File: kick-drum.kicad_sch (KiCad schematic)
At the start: 68 parts, among them J1 Conn_02x05_Odd_Even, J2 GATE, J3 ACCENT CV, J4 PITCH CV, J5 OUTPUT, M1 Standoff, M2 Standoff, M3 Screw, M4 Screw, M5 Screw, M6 Screw, Q1 BCM857DS,135, Q2 BC547C, Q3 BCM847DS,135, U1 TL074

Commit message: update footprints
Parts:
- removed H5, H6, H7, H8: Standoff, MountingHole:MountingHole_2.7mm_M2.5, symbol Mechanical:MountingHole
- removed M1, M2: Standoff, Eurorack:Standoff_M2.5x0.45-11mm, symbol Eurorack:Standoff
- removed M3, M4, M5, M6: Screw, Eurorack:Screw_M2.5x0.45-6mm, symbol Eurorack:Screw
- C10, C3, C4, C7, C8: footprint (none) -> Capacitor_SMD:C_0805_2012Metric
- C5, C6, C9: footprint (none) -> Capacitor_THT:C_Rect_L7.2mm_W3.5mm_P5.00mm_FKS2_FKP2_MKS2_MKP2
- D3, D4, D5, D6, D7: footprint (none) -> Diode_SMD:D_SOD-323_HandSoldering
- J2, J3, J4, J5: footprint (none) -> Eurorack:AudioJack2_Tayda_A-2566
- Q1, Q3: footprint (none) -> Package_SO:TSOP-6_1.65x3.05mm_P0.95mm
- Q2: footprint (none) -> Package_TO_SOT_THT:TO-92_Inline_Wide
- R10, R11, R12, R13, R14, R15, R16, R17, R18, R19, R20, R21, R3, R4, R5, R6, R7, R8, R9: footprint (none) -> Resistor_SMD:R_0805_2012Metric
- RV1, RV5, RV6, RV7: footprint (none) -> Eurorack:Potentiometer_RV16AF-41-15R1
- RV2, RV3, RV4: footprint (none) -> Potentiometer_THT:Potentiometer_Bourns_3296W_Vertical
- U1: footprint (none) -> Package_SO:SOIC-14-16_3.9x9.9mm_P1.27mm
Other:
- note removed: "Mechanical attachment for 3 layer module"

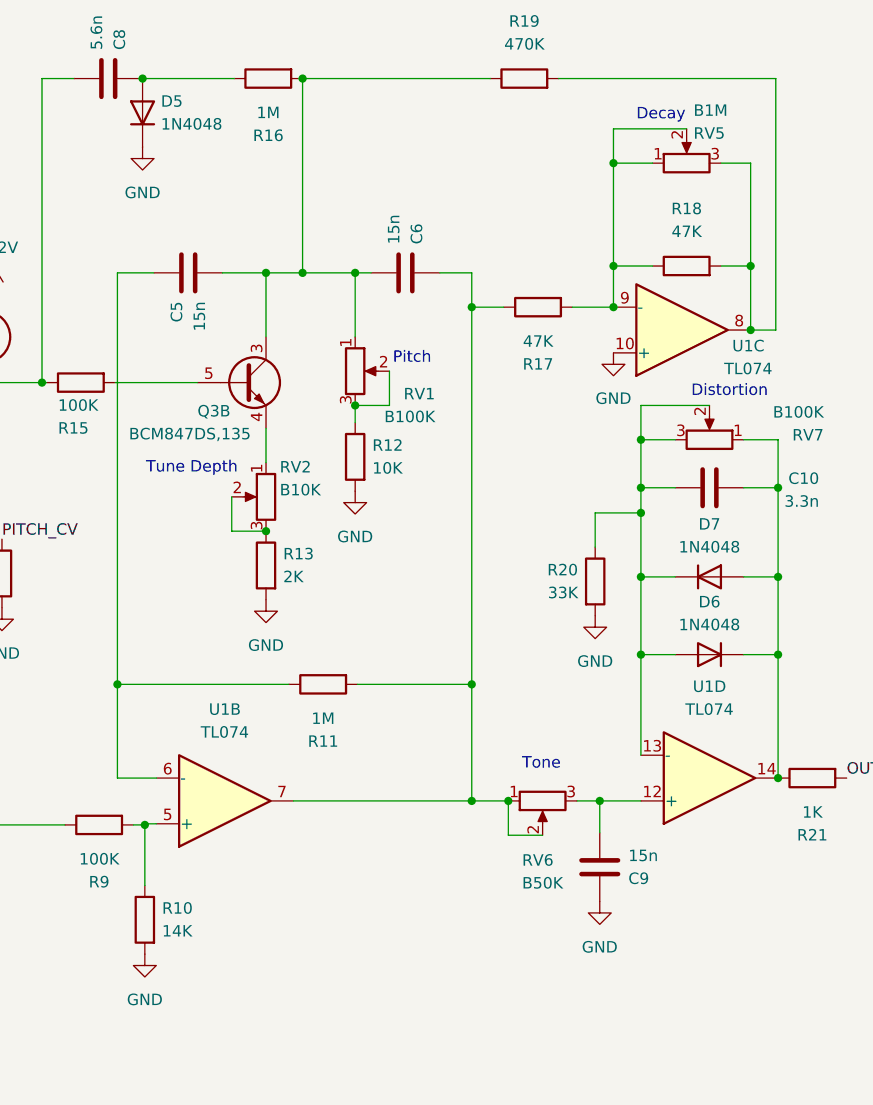
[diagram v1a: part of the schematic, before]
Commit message: update 15n caps to box type
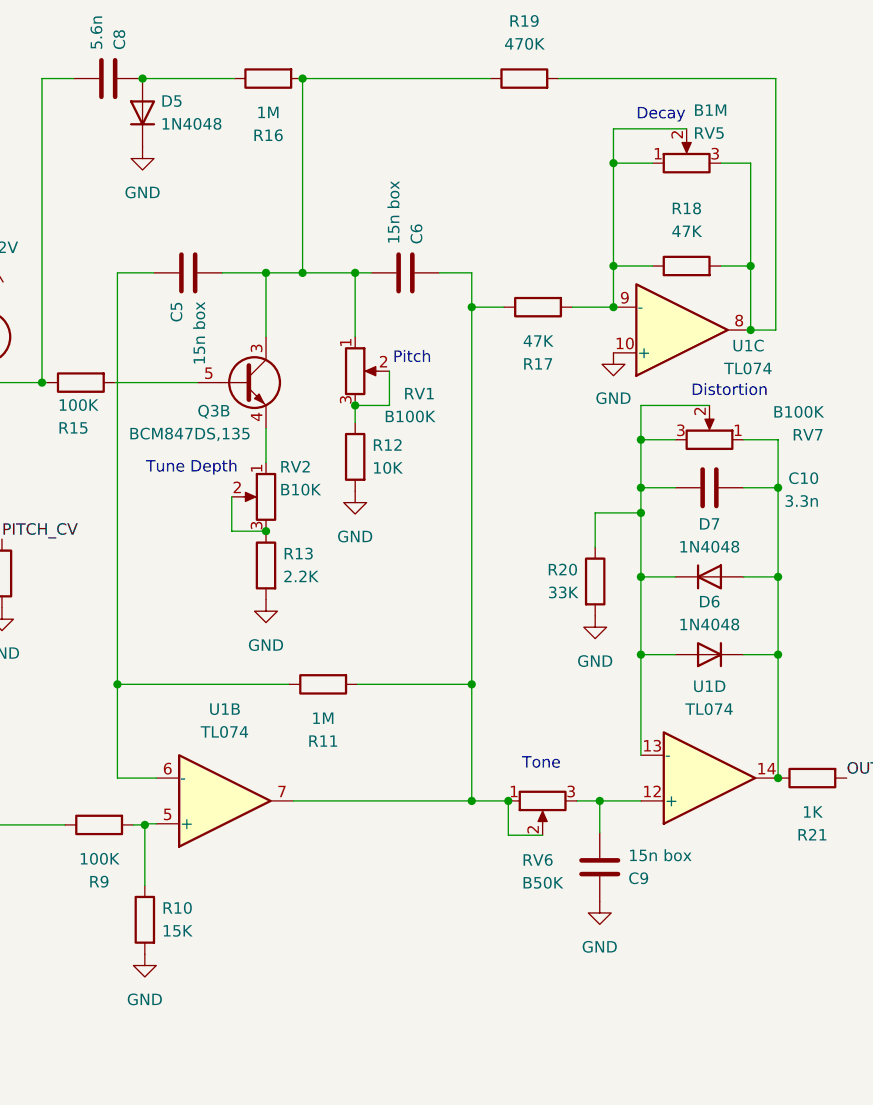
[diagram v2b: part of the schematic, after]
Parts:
- C5, C6, C9: value 15n -> 15n box
- R10: value 14K -> 15K
- R13: value 2K -> 2.2K
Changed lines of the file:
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@@
       (effects (font (size 1.27 1.27)) (justify right))
     )
-    (property "Value" "14K" (at 161.671 125.984 0)
+    (property "Value" "15K" (at 161.671 125.984 0)
       (effects (font (size 1.27 1.27)) (justify right))
     )
@@
       (effects (font (size 1.27 1.27)) (justify right))
     )
-    (property "Value" "15n" (at 187.452 49.657 0)
+    (property "Value" "15n box" (at 187.452 49.657 0)
       (effects (font (size 1.27 1.27)) (justify right))
     )
@@
       (effects (font (size 1.27 1.27)) (justify right))
     )
-    (property "Value" "15n" (at 213.487 117.602 0)
+    (property "Value" "15n box" (at 213.487 117.602 0)
       (effects (font (size 1.27 1.27)) (justify right))
     )
@@
       (effects (font (size 1.27 1.27)) (justify right))
     )
-    (property "Value" "15n" (at 165.862 56.007 0)
+    (property "Value" "15n box" (at 165.862 56.007 0)
       (effects (font (size 1.27 1.27)) (justify right))
     )
@@
       (effects (font (size 1.27 1.27)) (justify right))
     )
-    (property "Value" "2K" (at 175.133 86.614 0)
-      (effects (font (size 1.27 1.27)) (justify right))
-    )
+    (property "Value" "2.2K" (at 175.133 86.614 0)
+      (effects (font (size 1.27 1.27)) (justify right))
+    )

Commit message: bill of materials updates
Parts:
- D3, D4, D5, D6, D7: value 1N4048 -> 1N4148
- RV2: value B10K -> 10K
- RV3, RV4: value B100K -> 100K
- U1: PartNum (none) -> 595-TL074CDR; Vendor (none) -> Mouser
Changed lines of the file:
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@@
   (symbol (lib_id "Device:D") (at 222.504 95.25 180) (unit 1)
     (in_bom yes) (on_board yes) (dnp no) (fields_autoplaced)
-    (property "Reference" "D6" (at 222.504 89.408 0)
-      (effects (font (size 1.27 1.27)))
-    )
-    (property "Value" "1N4048" (at 222.504 91.948 0)
+    (property "Reference" "D6" (at 222.504 88.9 0)
+      (effects (font (size 1.27 1.27)))
+    )
+    (property "Value" "1N4148" (at 222.504 91.44 0)
       (effects (font (size 1.27 1.27)))
     )
@@
     )
     (property "Datasheet" "http://www.ti.com/lit/ds/symlink/tl071.pdf" (at 220.726 64.262 0)
+      (effects (font (size 1.27 1.27)) hide)
+    )
+    (property "Vendor" "Mouser" (at 219.456 59.182 0)
+      (effects (font (size 1.27 1.27)) hide)
+    )
+    (property "PartNum" "595-TL074CDR" (at 219.456 59.182 0)
       (effects (font (size 1.27 1.27)) hide)
     )
@@
   (symbol (lib_id "Device:D") (at 159.512 35.052 90) (unit 1)
     (in_bom yes) (on_board yes) (dnp no) (fields_autoplaced)
-    (property "Reference" "D5" (at 161.544 33.782 90)
-      (effects (font (size 1.27 1.27)) (justify right))
-    )
-    (property "Value" "1N4048" (at 161.544 36.322 90)
+    (property "Reference" "D5" (at 162.56 33.782 90)
+      (effects (font (size 1.27 1.27)) (justify right))
+    )
+    (property "Value" "1N4148" (at 162.56 36.322 90)
       (effects (font (size 1.27 1.27)) (justify right))
     )
@@
       (effects (font (size 1.27 1.27)) (justify left))
     )
-    (property "Value" "1N4048" (at 52.07 116.84 90)
+    (property "Value" "1N4148" (at 52.07 116.84 90)
       (effects (font (size 1.27 1.27)) (justify left))
     )
@@
       (effects (font (size 1.27 1.27)) (justify right))
     )
-    (property "Value" "B100K" (at 135.001 91.313 0)
+    (property "Value" "100K" (at 135.001 91.313 0)
       (effects (font (size 1.27 1.27)) (justify right))
     )
@@
   (symbol (lib_id "Device:D") (at 110.236 60.198 180) (unit 1)
     (in_bom yes) (on_board yes) (dnp no) (fields_autoplaced)
-    (property "Reference" "D4" (at 110.236 54.483 0)
-      (effects (font (size 1.27 1.27)))
-    )
-    (property "Value" "1N4048" (at 110.236 57.023 0)
+    (property "Reference" "D4" (at 110.236 54.61 0)
+      (effects (font (size 1.27 1.27)))
+    )
+    (property "Value" "1N4148" (at 110.236 57.15 0)
       (effects (font (size 1.27 1.27)))
     )
@@
       (effects (font (size 1.27 1.27)) (justify right))
     )
-    (property "Value" "B100K" (at 137.541 70.993 0)
+    (property "Value" "100K" (at 137.541 70.993 0)
       (effects (font (size 1.27 1.27)) (justify right))
     )
@@
   (symbol (lib_id "Device:D") (at 222.504 86.614 0) (unit 1)
     (in_bom yes) (on_board yes) (dnp no) (fields_autoplaced)
-    (property "Reference" "D7" (at 222.504 80.772 0)
-      (effects (font (size 1.27 1.27)))
-    )
-    (property "Value" "1N4048" (at 222.504 83.312 0)
+    (property "Reference" "D7" (at 222.504 80.01 0)
+      (effects (font (size 1.27 1.27)))
+    )
+    (property "Value" "1N4148" (at 222.504 82.55 0)
       (effects (font (size 1.27 1.27)))
     )
@@
     )
     (property "Datasheet" "http://www.ti.com/lit/ds/symlink/tl071.pdf" (at 223.774 114.046 0)
+      (effects (font (size 1.27 1.27)) hide)
+    )
+    (property "Vendor" "Mouser" (at 222.504 108.966 0)
+      (effects (font (size 1.27 1.27)) hide)
+    )
+    (property "PartNum" "595-TL074CDR" (at 222.504 108.966 0)
       (effects (font (size 1.27 1.27)) hide)
     )
@@
       (effects (font (size 1.27 1.27)) (justify right))
     )
-    (property "Value" "B10K" (at 174.752 76.962 0)
+    (property "Value" "10K" (at 174.752 76.962 0)
       (effects (font (size 1.27 1.27)) (justify right))
     )
@@
     )
     (property "Datasheet" "http://www.ti.com/lit/ds/symlink/tl071.pdf" (at 169.926 116.586 0)
+      (effects (font (size 1.27 1.27)) hide)
+    )
+    (property "Vendor" "Mouser" (at 168.656 111.506 0)
+      (effects (font (size 1.27 1.27)) hide)
+    )
+    (property "PartNum" "595-TL074CDR" (at 168.656 111.506 0)
       (effects (font (size 1.27 1.27)) hide)
     )
@@
       (effects (font (size 1.27 1.27)) hide)
     )
+    (property "Vendor" "Mouser" (at 65.405 109.22 0)
+      (effects (font (size 1.27 1.27)) hide)
+    )
+    (property "PartNum" "595-TL074CDR" (at 65.405 109.22 0)
+      (effects (font (size 1.27 1.27)) hide)
+    )
     (pin "1")
     (pin "6")
@@
       (effects (font (size 1.27 1.27)) hide)
     )
+    (property "Vendor" "Mouser" (at 277.495 153.035 0)
+      (effects (font (size 1.27 1.27)) hide)
+    )
+    (property "PartNum" "595-TL074CDR" (at 277.495 153.035 0)
+      (effects (font (size 1.27 1.27)) hide)
+    )

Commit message: prelim board layout
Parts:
- added H10: accent, Eurorack:Mech-AudioJack-Hole-Input-CV, symbol Mechanical:MountingHole_Pad
- added H11: pitch, Eurorack:Mech-AudioJack-Hole-Input-CV, symbol Mechanical:MountingHole_Pad
- added H12: out, Eurorack:Mech-AudioJack-Hole-Output, symbol Mechanical:MountingHole_Pad
- added H13: tune depth, Eurorack:Mech-LED-Hole-3mm, symbol Mechanical:MountingHole_Pad
- added H14: tune decay, Eurorack:Mech-LED-Hole-3mm, symbol Mechanical:MountingHole_Pad
- added H15: pitch cv, Eurorack:Mech-LED-Hole-3mm, symbol Mechanical:MountingHole_Pad
- added H5: tone, Eurorack:Mech-Potentiometer-Hole_level, symbol Mechanical:MountingHole_Pad
- added H6: decay, Eurorack:Mech-Potentiometer-Hole_level, symbol Mechanical:MountingHole_Pad
- added H7: dist, Eurorack:Mech-Potentiometer-Hole_level, symbol Mechanical:MountingHole_Pad
- added H8: pitch, Eurorack:Mech-Potentiometer-Hole_level, symbol Mechanical:MountingHole_Pad
- added H9: gate, Eurorack:Mech-AudioJack-Hole-Input-Gate, symbol Mechanical:MountingHole_Pad
- Q2: footprint Package_TO_SOT_THT:TO-92_Inline_Wide -> Package_TO_SOT_SMD:SOT-23-3; PartNum (none) -> 621-BC847C-13-F; Vendor (none) -> Mouser
- U1: footprint Package_SO:SOIC-14-16_3.9x9.9mm_P1.27mm -> Package_SO:SOIC-14_3.9x8.7mm_P1.27mm
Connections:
- net FACE: now also H10.1, H11.1, H12.1, H13.1, H14.1, H15.1, H5.1, H6.1, H7.1, H8.1, H9.1
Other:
- moved on the sheet: C10, C4, C5, C6, C7, C8, C9, D3, D4, D5, D6, D7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

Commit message: v0 ready
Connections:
- net at C10.2, D6.2 (A), D7.1 (K)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: now also RV7.1; no longer RV7.3
- net at C10.1, D6.1 (K), D7.2 (A)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: now also RV7.3; no longer RV7.1
- net at Q3.4 (E2): now also RV2.3; no longer RV2.1
- net at R13.1, RV2.2: now also RV2.1; no longer RV2.3
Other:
- moved on the sheet: RV2, RV7
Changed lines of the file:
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@@
     )
   )
-  (symbol (lib_id "Device:R_Potentiometer") (at 176.784 80.772 0) (mirror y) (unit 1)
-    (in_bom yes) (on_board yes) (dnp no)
-    (property "Reference" "RV2" (at 178.308 77.47 0)
-      (effects (font (size 1.27 1.27)) (justify right))
-    )
-    (property "Value" "10K" (at 178.308 80.01 0)
+  (symbol (lib_id "Device:R_Potentiometer") (at 176.784 80.772 180) (unit 1)
+    (in_bom yes) (on_board yes) (dnp no)
+    (property "Reference" "RV2" (at 178.308 84.074 0)
+      (effects (font (size 1.27 1.27)) (justify right))
+    )
+    (property "Value" "10K" (at 178.308 81.534 0)
       (effects (font (size 1.27 1.27)) (justify right))
     )
@@
     )
   )
-  (symbol (lib_id "Device:R_Potentiometer") (at 226.06 74.422 270) (mirror x) (unit 1)
-    (in_bom yes) (on_board yes) (dnp no)
-    (property "Reference" "RV7" (at 238.76 73.914 90)
-      (effects (font (size 1.27 1.27)) (justify right))
-    )
-    (property "Value" "B100K" (at 238.76 71.374 90)
-      (effects (font (size 1.27 1.27)) (justify right))
-    )
+  (symbol (lib_id "Device:R_Potentiometer") (at 226.06 74.422 90) (unit 1)
+    (in_bom yes) (on_board yes) (dnp no)
+    (property "Reference" "RV7" (at 233.68 72.39 90)
+      (effects (font (size 1.27 1.27)) (justify right))
+    )
+    (property "Value" "B100K" (at 233.68 69.85 90)
+      (effects (font (size 1.27 1.27)) (justify right))
+    )

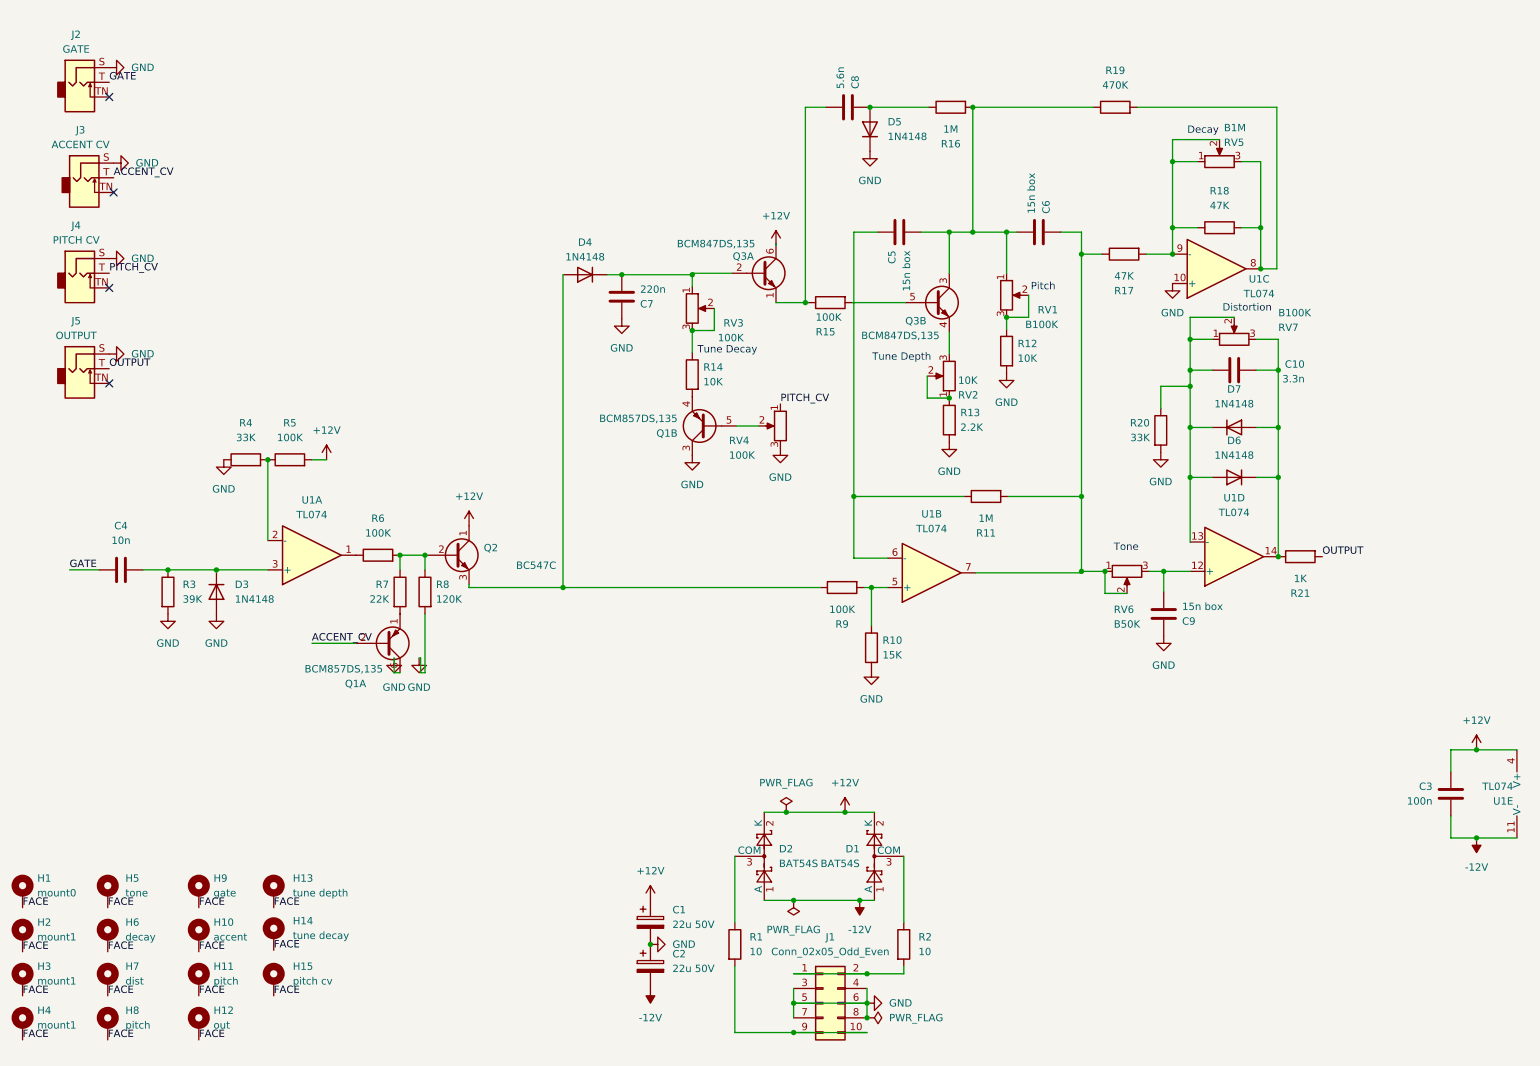
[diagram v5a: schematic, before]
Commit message: adding CV input protection
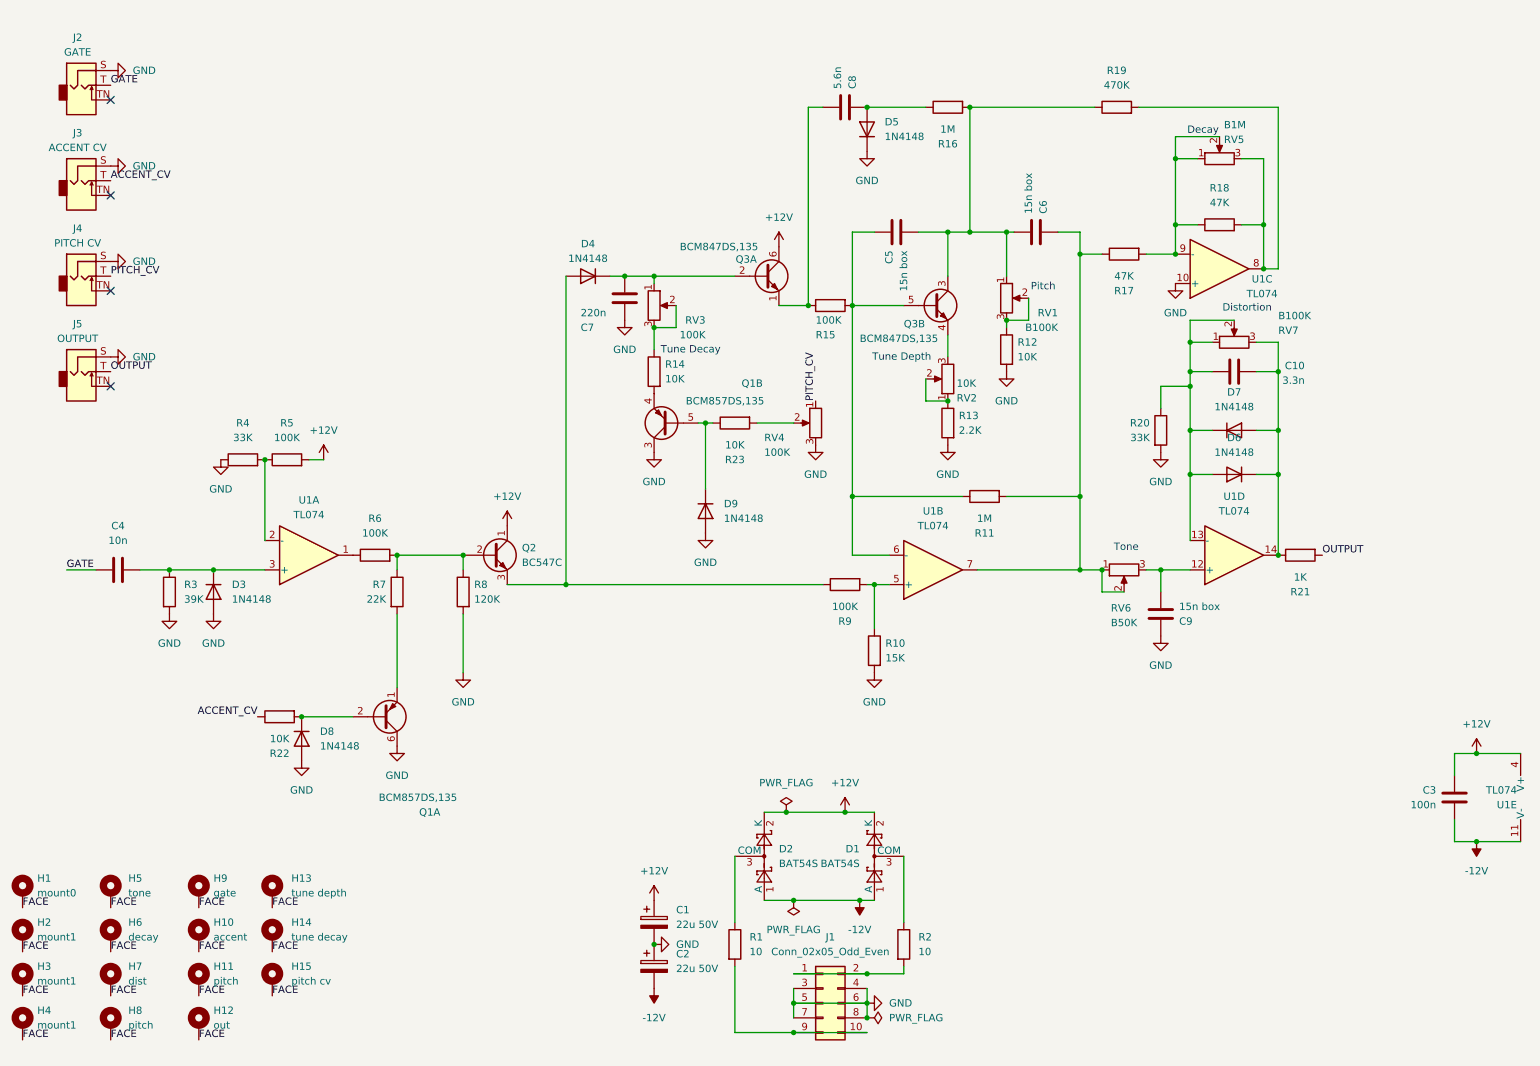
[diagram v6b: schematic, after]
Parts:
- added D8, D9: 1N4148, Diode_SMD:D_SOD-323_HandSoldering, symbol Device:D
- added R22, R23: 10K, Resistor_SMD:R_0805_2012Metric, symbol Device:R
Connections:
- net ACCENT_CV: now also R22.1; no longer Q1.2 (B1)
- net GND: now also D8.2 (A), D9.2 (A)
- net at Q3.5 (B2), R15.2: now also C5.1, R11.1, U1.6 (-)
- net at Q1.5 (B2): now also D9.1 (K), R23.1; no longer RV4.2
- new net: D8.1 (K), Q1.2 (B1), R22.2
- new net: R23.2, RV4.2
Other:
- moved on the sheet: C1, C2, C3, C4, C5, C6, C7, C8, C9, D3, D4, D5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
